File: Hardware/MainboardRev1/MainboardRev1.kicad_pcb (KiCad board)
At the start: 4 copper layers, 92 x 92 mm, 210 parts, among them J1 BACKUP_BATT: 1586038-2, J10 Switch_3, J11 Switch_2, J12 Switch_4, J13 EXTRA_5V, J14 EXTRA_3V3, J2 MAIN_BATT: 1586038-2, J3 Servo_Control, J4 EMATCH_1: 1586038-2, J5 EMATCH_2: 1586038-2, J6 Stratologger_PWR: 1586038-2, J7 Stratologger_DATA, J8 0733910320 [915MHz SMA], J9 Switch_1, Q1 SSM3J328R, Q10 SSM3J328R, Q11 NTR4003, Q12 NTR4003, Q13 NTR4003, Q14 SSM3J328R, Q15 NTR4003, Q16 SSM3J328R, Q17 SSM3J328R, Q18 NTR4003, Q19 NTR4003, Q2 SSM3J328R, Q20 SIS612EDNT-T1-GE3, Q21 SIS612EDNT-T1-GE3, Q22 NTR4003, Q23 NTR4003, Q24 NTR4003, Q25 SSM3J328R, Q26 NTR4003, Q3 SSM3J328R, Q4 SSM3J328R, Q5 NTR4003, Q6 NTR4003, Q7 NTR4003, Q8 SSM3J328R, Q9 NTR4003, SW1 EG2201A [DPDT], U1 LT6703-3, U10 LTC4358, U11 Teensy3.6, U12 ABPMANN030PG2A3, U13 LSM9DS1, U14 LIS331HH, U15 BME280, U16 CCS811, U17 ublox_max-m8q, U18 RFM69HCW, U2 LTC3605, U3 LTC4358, U4 LTC4358, U5 LDL1117S50R, U6 LDL1117S33R, U7 LTC2992, U8 LDL1117S33R, U9 LTC2992

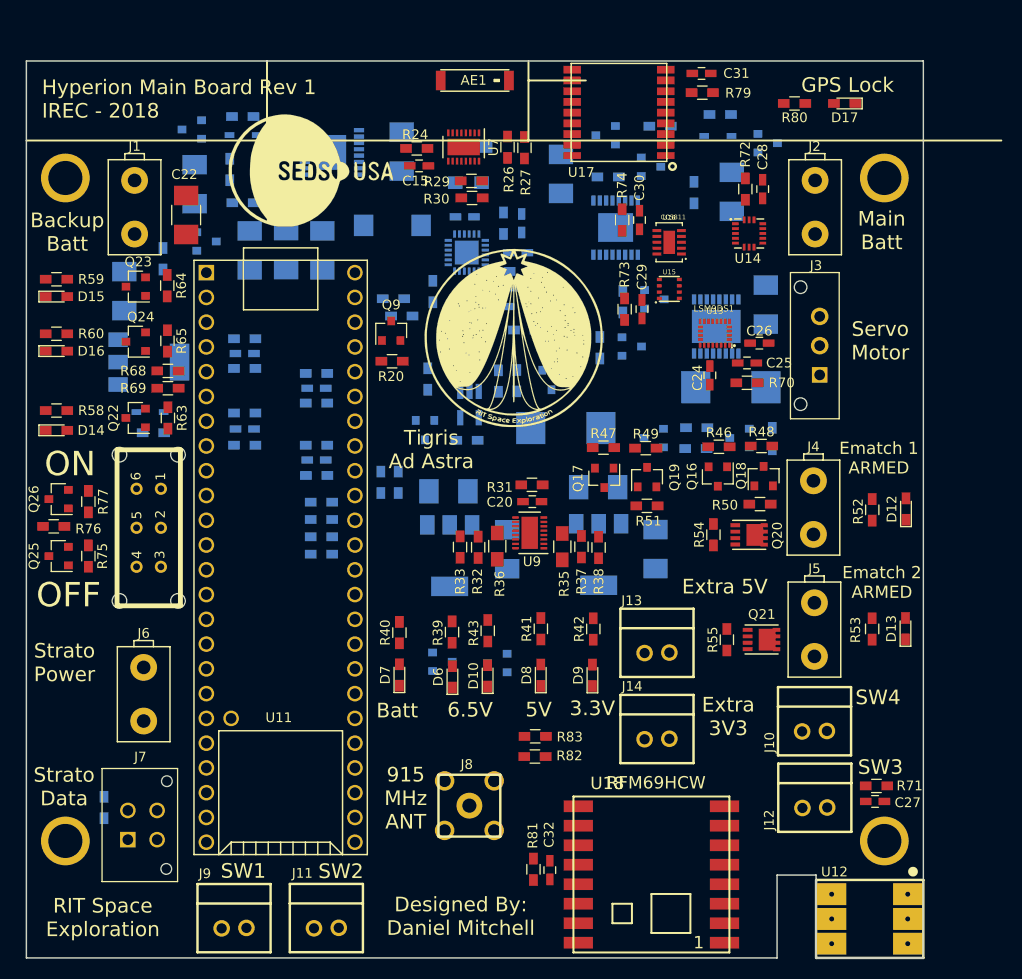
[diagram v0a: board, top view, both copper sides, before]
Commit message: Added buzzer and strobe LED. Created BOM. Reannotated. Added sponsors to silkscreen. Needs to be routed and sent out. Good luck Matt!
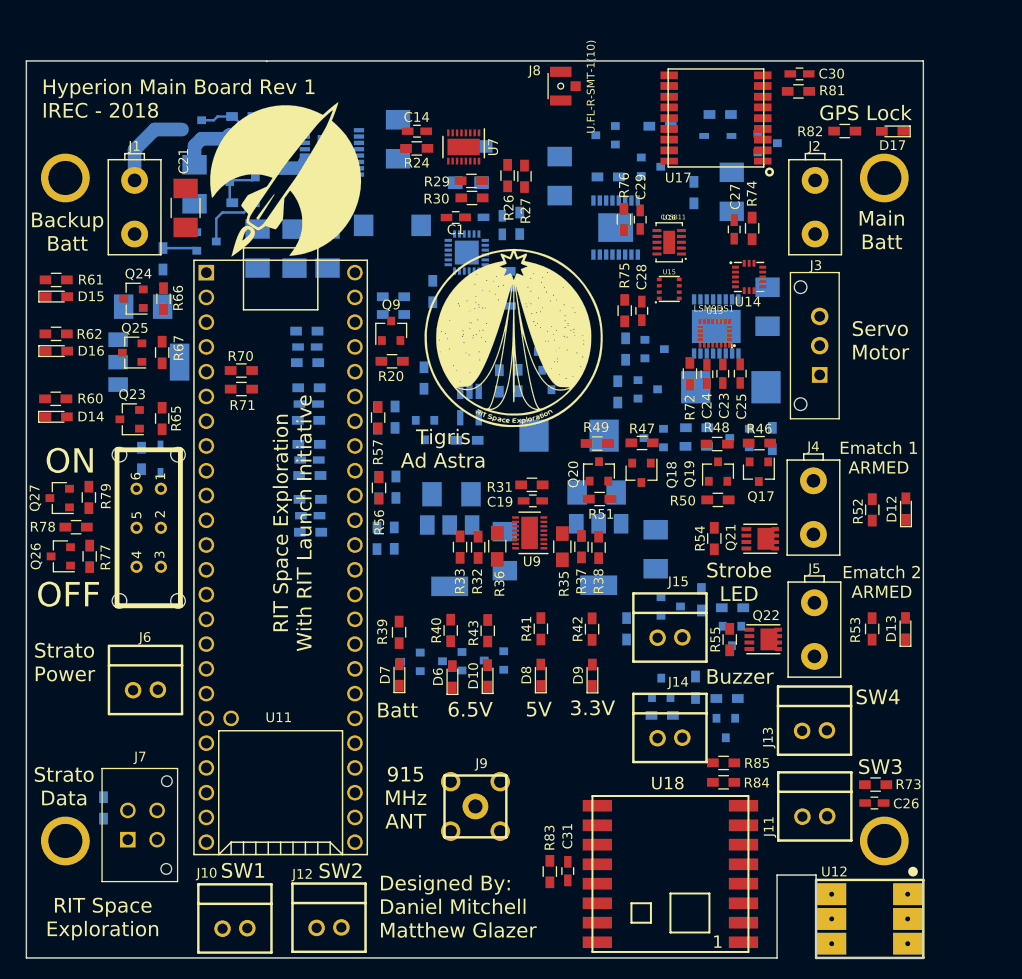
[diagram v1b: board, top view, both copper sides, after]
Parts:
- removed AE1: 1575AT43A0040E, Dans_Parts:ANT_CHIP_OMNI_1575MHz_GPS
- removed C36: 10nF, Capacitors_SMD:C_0603_HandSoldering
- added C1: 0.1uF, Capacitors_SMD:C_0603_HandSoldering, F.Cu at (94.0, 66.1)
- added G***: LOGO, Media:LI_Logo, F.Cu at (76.6, 62.1)
- added J15: Strobe, Dans_Parts:CONN_2POS_VERT_TE_CONN_LOCK_5-103669-1, F.Cu at (116.0, 109.1)
- added Q27: NTR4003, TO_SOT_Packages_SMD:SOT-23, F.Cu at (53.4, 94.8)
- added Q28: SSM3J328R, TO_SOT_Packages_SMD:SOT-23, B.Cu at (121.7, 118.4)
- added Q29: SSM3J328R, TO_SOT_Packages_SMD:SOT-23, B.Cu at (122.4, 109.0)
- added Q30: NTR4003, TO_SOT_Packages_SMD:SOT-23, B.Cu at (115.1, 114.3)
- added Q31: NTR4003, TO_SOT_Packages_SMD:SOT-23, B.Cu at (116.1, 106.0)
- added R92: 1k, Resistors_SMD:R_0603_HandSoldering, B.Cu at (79.0, 89.3)
- added R93: 1k, Resistors_SMD:R_0603_HandSoldering, B.Cu at (78.8, 77.7)
- added R94: 10K, Resistors_SMD:R_0603_HandSoldering, B.Cu at (121.9, 115.4)
- added R95: 10K, Resistors_SMD:R_0603_HandSoldering, B.Cu at (122.4, 106.1)
- added R96: 12k, Resistors_SMD:R_0603_HandSoldering, B.Cu at (118.6, 114.2)
- added R97: 12k, Resistors_SMD:R_0603_HandSoldering, B.Cu at (119.2, 105.3)
- added R98: 10k, Resistors_SMD:R_0603_HandSoldering, B.Cu at (115.2, 117.1)
- added R99: 10k, Resistors_SMD:R_0603_HandSoldering, B.Cu at (111.6, 108.2)
- C14, C19: value 47uF -> 0.1uF; footprint Capacitors_SMD:C_1210_HandSoldering -> Capacitors_SMD:C_0603_HandSoldering; moved to F.Cu
- C15, C20: value 0.1uF -> 47uF; footprint Capacitors_SMD:C_0603_HandSoldering -> Capacitors_SMD:C_1210_HandSoldering; moved to B.Cu
- C21, R84, R85: moved to F.Cu
- C22, G***: moved to B.Cu
- C23: value 47uF -> 10000pF; footprint Capacitors_SMD:C_1210_HandSoldering -> Capacitors_SMD:C_0603_HandSoldering; moved to F.Cu
- C24: value 10000pF -> 0.1uF
- C25: value 0.1uF -> 100nF
- C26: value 100nF -> 0.1uF
- C32: value 0.1uF -> 10nF; moved to B.Cu
- C4: value 0.1uF -> .01uF
- C5: value .01uF -> 0.1uF
- C7: value 0.1uF -> 10pF
- C8: value 10pF -> 220pF
- C9: value 220pF -> 47uF; footprint Capacitors_SMD:C_0603_HandSoldering -> Capacitors_SMD:C_1210_HandSoldering
- D14: value LED -> Green
- D15: value LED -> Blue
- D16: value LED -> Red
- J10: value Switch_3 -> Switch_1
- J11: value Switch_2 -> Switch_3
- J12: value Switch_4 -> Switch_2
- J13: value EXTRA_5V -> Switch_4
- J14: value EXTRA_3V3 -> Buzzer
- J6: footprint Dans_Parts:CONN_2POS_VERT_TE_CONN -> Dans_Parts:CONN_2POS_VERT_TE_CONN_LOCK_5-103669-1
- J8: value 0733910320 [915MHz SMA] -> U.FL-R-SMT-1(10); footprint Dans_Parts:CONN_RP-SMA_Right_Angle_0733910320 -> Dans_Parts:HRS_U.FL-R-SMT-1(10)
- J9: value Switch_1 -> 0733910320 [915MHz SMA]; footprint Dans_Parts:CONN_2POS_VERT_TE_CONN_LOCK_5-103669-1 -> Dans_Parts:CONN_RP-SMA_Right_Angle_0733910320
- Q14, Q25: value SSM3J328R -> NTR4003
- Q15, Q18, Q26: value NTR4003 -> SSM3J328R
- Q16: value SSM3J328R -> NTR4003; moved to B.Cu
- Q20: value SIS612EDNT-T1-GE3 -> NTR4003; footprint Dans_Parts:PowerPAK_1212-8S -> TO_SOT_Packages_SMD:SOT-23
- Q22: value NTR4003 -> SIS612EDNT-T1-GE3; footprint TO_SOT_Packages_SMD:SOT-23 -> Dans_Parts:PowerPAK_1212-8S
- R14, R9: value 500 -> 510
- R39, R40, R42, R60: value R -> 80
- R41: value R -> 470
- R43: value R -> 150
- R52, R53: value R -> 510
- R56: value 45.2k -> 1M; moved to F.Cu
- R57: value 11.3k -> 1M; moved to F.Cu
- R58: value R -> 45.3k; moved to B.Cu
- R59: value R -> 11.3k; moved to B.Cu
- R61: value 45.2k -> 80; moved to F.Cu
- R62: value 11.3k -> 150; moved to F.Cu
- R63, R68: value 10k -> 45.3k; moved to B.Cu
- R64, R69: value 10k -> 11.3k; moved to B.Cu
- R66: value 45.2k -> 10k; moved to F.Cu
- R67: value 11.3k -> 10k; moved to F.Cu
- R70, R71, R79: value 10 -> 10k
- R75, R83: value 10k -> 10
- R76: value 12k -> 10
- R78: value 0 -> 12k; moved to F.Cu
- R80: value R -> 0; moved to B.Cu
- R82: value 10k -> 80
- R86, R87, R90, R91: value 1k -> 10k
- R88, R89: value 10k -> 1k
- moved R80 101.2 mm to (57.9, 126.6), turned to 90 degrees
- moved R81 84.3 mm to (129.2, 53.1), turned to 0 degrees
- moved C31 83.0 mm to (105.5, 133.1), turned to 90 degrees
- moved R71 76.8 mm to (72.1, 83.7), turned to 180 degrees
- moved R79 75.4 mm to (56.4, 94.8), turned to 90 degrees
- moved J8 74.4 mm to (104.8, 52.6), turned to 90 degrees
- moved R82 71.6 mm to (133.9, 57.2)
- moved Q22 66.6 mm to (124.2, 108.3), turned to 0 degrees
- moved R76 66.4 mm to (111.3, 66.3), turned to 90 degrees
- moved J10 62.8 mm to (71.4, 138.9)
- moved G*** 61.0 mm to (101.7, 117.9), turned to 180 degrees
- moved R75 60.5 mm to (111.4, 75.6)
- moved C27 60.4 mm to (122.6, 67.3), turned to 90 degrees
- moved C22 60.4 mm to (126.0, 75.2)
- moved R85 55.7 mm to (121.5, 122.0), turned to 0 degrees
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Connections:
- C11 pad 1: +6.5V_MSMT -> BATTERY_PWR_MSMT
- C12 pad 1: BATTERY_PWR_MSMT -> +6.5V_MSMT
- C13 pad 1: +6.5V_MSMT -> BATTERY_PWR_MSMT
- C14 pad 1: BATTERY_PWR_MSMT -> Net-(C14-Pad1)
- C15 pad 1: Net-(C15-Pad1) -> LDO_FEED
- C17 pad 1: LDO_FEED -> +5V_MSMT
- C18 pad 1: +5V_MSMT -> +3.3V_MSMT
- C19 pad 1: +3.3V_MSMT -> Net-(C19-Pad1)
- C20 pad 1: Net-(C20-Pad1) -> STARTUP_BATT
- C21 pad 1: STARTUP_BATT -> +3.3V_STARTUP
- C22 pad 1: +3.3V_STARTUP -> Net-(C22-Pad1)
- C23 pad 1: Net-(C23-Pad1) -> LSM_CAP
- C24 pad 1: LSM_CAP -> Net-(C24-Pad1)
- C25 pad 1: Net-(C25-Pad1) -> LSM_C1
- C26 pad 1: LSM_C1 -> Net-(C26-Pad1)
- C4 pad 1: BATTERY_PWR -> Net-(C4-Pad1)
- C5 pad 1: Net-(C5-Pad1) -> GND
- C5 pad 2: GND -> SVIN
- C6 pad 1: GND -> Net-(C6-Pad1)
- C6 pad 2: SVIN -> Net-(C6-Pad2)
- C7 pad 2: Net-(C7-Pad2) -> GND
- C9 pad 1: Net-(C9-Pad1) -> +6.5V_MSMT
- D11 pad 1: Net-(C23-Pad1) -> Net-(C22-Pad1)
- D3 pad 1: Net-(C7-Pad1) -> Net-(C6-Pad1)
- D7 pad 1: GND -> Net-(D7-Pad1)
- J10 pad 1: Net-(C34-Pad1) -> Net-(C32-Pad1)
- J11 pad 1: Net-(C35-Pad1) -> Net-(C33-Pad1)
- J12 pad 1: Net-(C36-Pad1) -> Net-(C34-Pad1)
- J13 pad 1: GND -> Net-(C35-Pad1)
- J13 pad 2: +5V -> GND
- J14 pad 1: GND -> Net-(J14-Pad1)
- J14 pad 2: +3.3V -> GND
- J3 pad 2: Net-(C23-Pad1) -> Net-(C22-Pad1)
- J9 pad 1: Net-(C33-Pad1) -> Net-(J9-Pad1)
- L1 pad 1: Net-(C7-Pad2) -> Net-(C6-Pad2)
- Q13 pad 1: CONTROL_2 -> +3.3V
- Q13 pad 3: Net-(D10-Pad1) -> Net-(D7-Pad1)
- Q14 pad 1: Net-(Q14-Pad1) -> CONTROL_2
- Q14 pad 2: +6.5V -> GND
- Q14 pad 3: Net-(Q14-Pad3) -> Net-(D10-Pad1)
- Q15 pad 1: SERVO_PWR_EN -> Net-(Q15-Pad1)
- Q15 pad 2: GND -> +6.5V
- Q15 pad 3: Net-(Q14-Pad1) -> Net-(Q15-Pad3)
- Q16 pad 1: Net-(Q16-Pad1) -> SERVO_PWR_EN
- Q16 pad 2: BATTERY_PWR -> GND
- Q16 pad 3: Net-(J4-Pad1) -> Net-(Q15-Pad1)
- Q17 pad 3: Net-(J5-Pad1) -> Net-(J4-Pad1)
- Q18 pad 1: EMATCH_1_ARM -> Net-(Q18-Pad1)
- Q18 pad 2: GND -> BATTERY_PWR
- Q18 pad 3: Net-(Q18-Pad3) -> Net-(J5-Pad1)
- Q19 pad 1: EMATCH_2_ARM -> EMATCH_1_ARM
- Q20 pad 1: EMATCH_1_FIRE -> EMATCH_2_ARM
- Q20 pad 3: EMATCH_1_CHECK -> Net-(Q20-Pad3)
- Q21 pad 1: EMATCH_2_FIRE -> EMATCH_1_FIRE
- Q21 pad 3: EMATCH_2_CHECK -> EMATCH_1_CHECK
- Q22 pad 1: LED_GREEN -> EMATCH_2_FIRE
- Q22 pad 3: Net-(D14-Pad1) -> EMATCH_2_CHECK
- Q23 pad 1: LED_BLUE -> LED_GREEN
- Q23 pad 3: Net-(D15-Pad1) -> Net-(D14-Pad1)
- Q24 pad 1: LED_RED -> LED_BLUE
- Q24 pad 3: Net-(D16-Pad1) -> Net-(D15-Pad1)
- Q25 pad 1: Net-(Q25-Pad1) -> LED_RED
- Q25 pad 2: BACKUP_BATT -> GND
- Q25 pad 3: Net-(J6-Pad1) -> Net-(D16-Pad1)
- Q26 pad 1: +3.3V_STARTUP -> Net-(Q26-Pad1)
- Q26 pad 2: GND -> BACKUP_BATT
- Q26 pad 3: Net-(Q26-Pad3) -> Net-(J6-Pad1)
- R15 pad 1: Net-(C9-Pad1) -> Net-(C8-Pad1)
- R15 pad 2: Net-(C8-Pad1) -> Net-(C7-Pad1)
- R24 pad 1: Net-(C15-Pad1) -> Net-(C14-Pad1)
- R31 pad 1: Net-(C20-Pad1) -> Net-(C19-Pad1)
- R39 pad 1: +5V -> Net-(D7-Pad2)
- R39 pad 2: Net-(D6-Pad2) -> +5V
- R40 pad 1: Net-(D7-Pad2) -> +5V
- R40 pad 2: BATTERY_PWR -> Net-(D6-Pad2)
- R41 pad 2: +5V -> BATTERY_PWR
- R42 pad 2: +3.3V -> +5V
- R44 pad 2: Net-(Q14-Pad1) -> Net-(Q15-Pad1)
- R46 pad 2: Net-(Q16-Pad1) -> Net-(Q17-Pad1)
- R47 pad 2: Net-(Q17-Pad1) -> Net-(Q18-Pad1)
- R48 pad 1: Net-(Q16-Pad1) -> Net-(Q17-Pad1)
- R48 pad 2: Net-(Q18-Pad3) -> Net-(Q19-Pad3)
- R49 pad 1: Net-(Q17-Pad1) -> Net-(Q18-Pad1)
- R49 pad 2: Net-(Q19-Pad3) -> Net-(Q20-Pad3)
- R56 pad 1: MAIN_BATT -> EMATCH_1_CHECK
- R56 pad 2: MAIN_BATT_ANLG -> GND
- R57 pad 1: MAIN_BATT_ANLG -> EMATCH_2_CHECK
- R57 pad 2: MAIN_BATT_READ_EN -> GND
- R58 pad 1: Net-(D14-Pad2) -> MAIN_BATT
- R58 pad 2: +5V -> MAIN_BATT_ANLG
- R59 pad 1: Net-(D15-Pad2) -> MAIN_BATT_ANLG
- R59 pad 2: +5V -> MAIN_BATT_READ_EN
- R60 pad 1: Net-(D16-Pad2) -> Net-(D14-Pad2)
- R61 pad 1: EMATCH_1_CHECK -> Net-(D15-Pad2)
- R61 pad 2: EMATCH_1_ANLG -> +5V
- R62 pad 1: EMATCH_1_ANLG -> Net-(D16-Pad2)
- R62 pad 2: GND -> +5V
- R63 pad 1: GND -> EMATCH_1_CHECK
- R63 pad 2: LED_GREEN -> EMATCH_1_ANLG
- R64 pad 1: GND -> EMATCH_1_ANLG
- R64 pad 2: LED_BLUE -> GND
- R65 pad 1: +3.3V -> GND
- R65 pad 2: LED_RED -> LED_GREEN
- R66 pad 1: EMATCH_2_CHECK -> GND
- R66 pad 2: EMATCH_2_ANLG -> LED_BLUE
- R67 pad 1: EMATCH_2_ANLG -> +3.3V
- R67 pad 2: GND -> LED_RED
- R68 pad 1: +3.3V -> EMATCH_2_CHECK
- R68 pad 2: SENSORS_SCL -> EMATCH_2_ANLG
- R69 pad 1: +3.3V -> EMATCH_2_ANLG
- R69 pad 2: SENSORS_SDA -> GND
- R70 pad 1: Net-(C25-Pad1) -> +3.3V
- R70 pad 2: +3.3V -> SENSORS_SCL
- R71 pad 1: Net-(C27-Pad1) -> +3.3V
- R71 pad 2: +3.3V -> SENSORS_SDA
- R72 pad 1: Net-(C28-Pad1) -> Net-(C24-Pad1)
- R73 pad 1: Net-(C29-Pad1) -> Net-(C26-Pad1)
- R74 pad 1: Net-(C30-Pad1) -> Net-(C27-Pad1)
- R75 pad 1: BACKUP_BATT -> Net-(C28-Pad1)
- R75 pad 2: Net-(Q25-Pad1) -> +3.3V
- R76 pad 1: Net-(Q25-Pad1) -> Net-(C29-Pad1)
- R76 pad 2: Net-(Q26-Pad3) -> +3.3V
- R77 pad 1: +3.3V_STARTUP -> BACKUP_BATT
- R77 pad 2: GND -> Net-(Q26-Pad1)
- R78 pad 1: Net-(J7-Pad1) -> Net-(Q26-Pad1)
- R78 pad 2: +3.3V -> Net-(Q27-Pad3)
- R79 pad 1: Net-(C31-Pad1) -> +3.3V_STARTUP
- R79 pad 2: +3.3V -> GND
- R80 pad 1: Net-(D17-Pad2) -> Net-(J7-Pad1)
- R80 pad 2: Net-(R80-Pad2) -> +3.3V
- R81 pad 1: Net-(C32-Pad1) -> Net-(C30-Pad1)
- R82 pad 1: +3.3V -> Net-(D17-Pad2)
- R82 pad 2: COMMS_CS_LORA -> Net-(R82-Pad2)
- R83 pad 1: +3.3V -> Net-(C31-Pad1)
- R83 pad 2: LORA_RESET -> +3.3V
- R84 pad 2: Net-(C33-Pad1) -> COMMS_CS_LORA
- R85 pad 2: Net-(C34-Pad1) -> LORA_RESET
- R86 pad 1: SWITCH_1 -> +3.3V
- R86 pad 2: Net-(C33-Pad1) -> Net-(C32-Pad1)
- R87 pad 1: SWITCH_3 -> +3.3V
- R87 pad 2: Net-(C34-Pad1) -> Net-(C33-Pad1)
- R88 pad 1: +3.3V -> SWITCH_1
- R88 pad 2: Net-(C35-Pad1) -> Net-(C32-Pad1)
- R89 pad 1: +3.3V -> SWITCH_3
- R89 pad 2: Net-(C36-Pad1) -> Net-(C33-Pad1)
- R90 pad 1: SWITCH_2 -> +3.3V
- R90 pad 2: Net-(C35-Pad1) -> Net-(C34-Pad1)
- R91 pad 1: SWITCH_4 -> +3.3V
- R91 pad 2: Net-(C36-Pad1) -> Net-(C35-Pad1)
- U10 pad 1: Net-(Q14-Pad3) -> Net-(Q15-Pad3)
- U10 pad 10: Net-(C23-Pad1) -> Net-(C22-Pad1)
- U10 pad 12: Net-(Q14-Pad3) -> Net-(Q15-Pad3)
- U10 pad 13: Net-(Q14-Pad3) -> Net-(Q15-Pad3)
- U10 pad 14: Net-(Q14-Pad3) -> Net-(Q15-Pad3)
- U10 pad 15: Net-(Q14-Pad3) -> Net-(Q15-Pad3)
- U10 pad 16: Net-(Q14-Pad3) -> Net-(Q15-Pad3)
- U10 pad 17: Net-(C23-Pad1) -> Net-(C22-Pad1)
- U10 pad 2: Net-(Q14-Pad3) -> Net-(Q15-Pad3)
- U10 pad 3: Net-(Q14-Pad3) -> Net-(Q15-Pad3)
- U10 pad 4: Net-(Q14-Pad3) -> Net-(Q15-Pad3)
- U10 pad 9: Net-(C23-Pad1) -> Net-(C22-Pad1)
- U11 pad 34: DATA_READY -> Buzzer_Disable
- U11 pad 35: DATA_READY_1 -> Strobe_Disable
- U12 pad 2: Net-(C27-Pad1) -> Net-(C26-Pad1)
- U13 pad 1: Net-(C25-Pad1) -> Net-(C24-Pad1)
- U13 pad 22: Net-(C25-Pad1) -> Net-(C24-Pad1)
- U13 pad 23: Net-(C25-Pad1) -> Net-(C24-Pad1)
- U13 pad 3: Net-(C25-Pad1) -> Net-(C24-Pad1)
- U14 pad 1: Net-(C28-Pad1) -> Net-(C27-Pad1)
- U14 pad 14: Net-(C28-Pad1) -> Net-(C27-Pad1)
- U14 pad 15: Net-(C28-Pad1) -> Net-(C27-Pad1)
- U15 pad 2: Net-(C29-Pad1) -> Net-(C28-Pad1)
- U15 pad 6: Net-(C29-Pad1) -> Net-(C28-Pad1)
- U15 pad 8: Net-(C29-Pad1) -> Net-(C28-Pad1)
- U16 pad 6: Net-(C30-Pad1) -> Net-(C29-Pad1)
- U17 pad 11: Net-(AE1-Pad1) -> Net-(J8-Pad1)
- U17 pad 4: Net-(R80-Pad2) -> Net-(R82-Pad2)
- U17 pad 6: Net-(C31-Pad1) -> Net-(C30-Pad1)
- U17 pad 7: Net-(C31-Pad1) -> Net-(C30-Pad1)
- U17 pad 8: Net-(C31-Pad1) -> Net-(C30-Pad1)
- U17 pad 9: Net-(C31-Pad1) -> Net-(C30-Pad1)
- U18 pad 13: Net-(C32-Pad1) -> Net-(C31-Pad1)
- U18 pad 9: Net-(J8-Pad1) -> Net-(J9-Pad1)
- U2 pad 11: Net-(C7-Pad2) -> Net-(C6-Pad2)
- U2 pad 12: Net-(C7-Pad2) -> Net-(C6-Pad2)
- U2 pad 13: Net-(C7-Pad2) -> Net-(C6-Pad2)
- U2 pad 14: Net-(C7-Pad2) -> Net-(C6-Pad2)
- U2 pad 15: Net-(C7-Pad2) -> Net-(C6-Pad2)
- U2 pad 16: Net-(C7-Pad2) -> Net-(C6-Pad2)
- U2 pad 20: Net-(C7-Pad1) -> Net-(C6-Pad1)
- U2 pad 5: Net-(C5-Pad1) -> Net-(C4-Pad1)
- U2 pad 6: Net-(C8-Pad1) -> Net-(C7-Pad1)
- U7 pad 4: DATA_READY -> Net-(U7-Pad4)
- U7 pad 7: Net-(C15-Pad1) -> Net-(C14-Pad1)
- U7 pad 8: Net-(C15-Pad1) -> Net-(C14-Pad1)
- U9 pad 4: DATA_READY_1 -> Net-(U9-Pad4)
- U9 pad 7: Net-(C20-Pad1) -> Net-(C19-Pad1)
- U9 pad 8: Net-(C20-Pad1) -> Net-(C19-Pad1)
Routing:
- net BACKUP_BATT: track 0.00 -> 11.1 mm
- net Net-(J1-Pad1): track 0.00 -> 8.88 mm
- net Net-(Q5-Pad3): track 0.00 -> 6.86 mm
- net Net-(D1-Pad2): track 0.00 -> 6.60 mm
- net GND: track 0.00 -> 5.86 mm
- net Net-(Q3-Pad1): track 0.00 -> 5.17 mm
- net Net-(Q3-Pad3): track 0.00 -> 5.03 mm
- net BACKUP_BATT_EN: track 0.00 -> 3.58 mm
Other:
- board text added: "Buzzer"
- board text added: "Designed By: Daniel Mitchell Matthew Glazer"
- board text added: "RIT Space Exploration With RIT Launch Initiative"
- board text added: "Sponsored By: SEDS USA Matthew Glazer Samuel Carlson SPEXcast"
- board text added: "Strobe LED"
- board text removed: "Designed By: Daniel Mitchell"
- board text removed: "Extra 3V3"
- board text removed: "Extra 5V"

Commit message: started routing PCB
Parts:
- moved R10 1.76 mm to (70.9, 65.7), turned to 270 degrees
- moved Q5 0.30 mm to (68.2, 68.4)
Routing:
- net Net-(C26-Pad1): track 0.00 -> 21.9 mm
- net Net-(J6-Pad1): track 0.00 -> 19.6 mm
- net BACKUP_BATT: track 11.1 -> 21.1 mm
- net Net-(D15-Pad1): track 0.00 -> 8.80 mm
- net Net-(D14-Pad1): track 0.00 -> 8.62 mm
- net Net-(D16-Pad1): track 0.00 -> 8.60 mm
- net Net-(R82-Pad2): track 0.00 -> 7.40 mm
- net Net-(Q27-Pad3): track 0.00 -> 5.73 mm
- net Net-(Q26-Pad1): track 0.00 -> 4.62 mm
- net Net-(Q5-Pad3): track 6.86 -> 2.36 mm
- net Net-(J7-Pad1): track 0.00 -> 4.32 mm
- net Net-(D12-Pad2): track 0.00 -> 3.49 mm
- net Net-(D13-Pad2): track 0.00 -> 3.43 mm
- net Net-(D17-Pad2): track 0.00 -> 2.72 mm
- net +3.3V_STARTUP: track 0.00 -> 2.03 mm
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
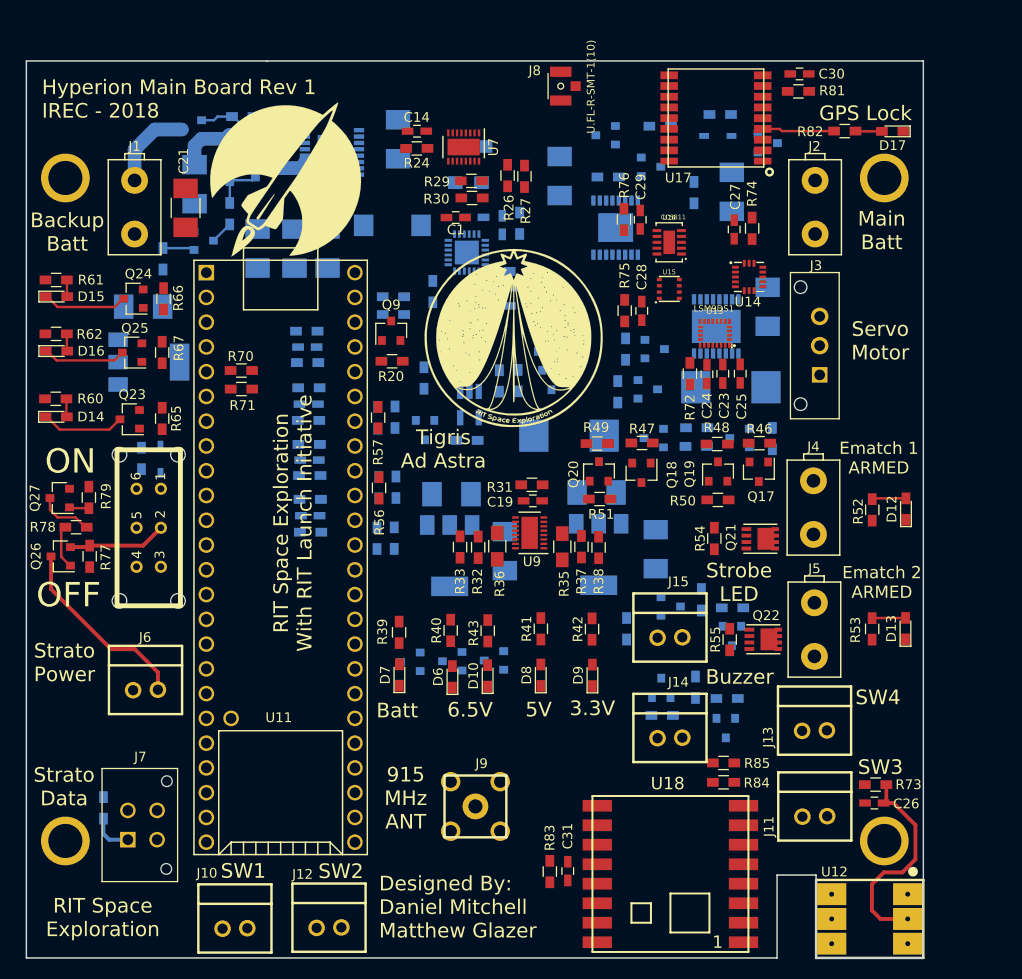
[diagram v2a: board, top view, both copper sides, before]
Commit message: continued work on routing, plenty of work still to be done
commiting my work for the night
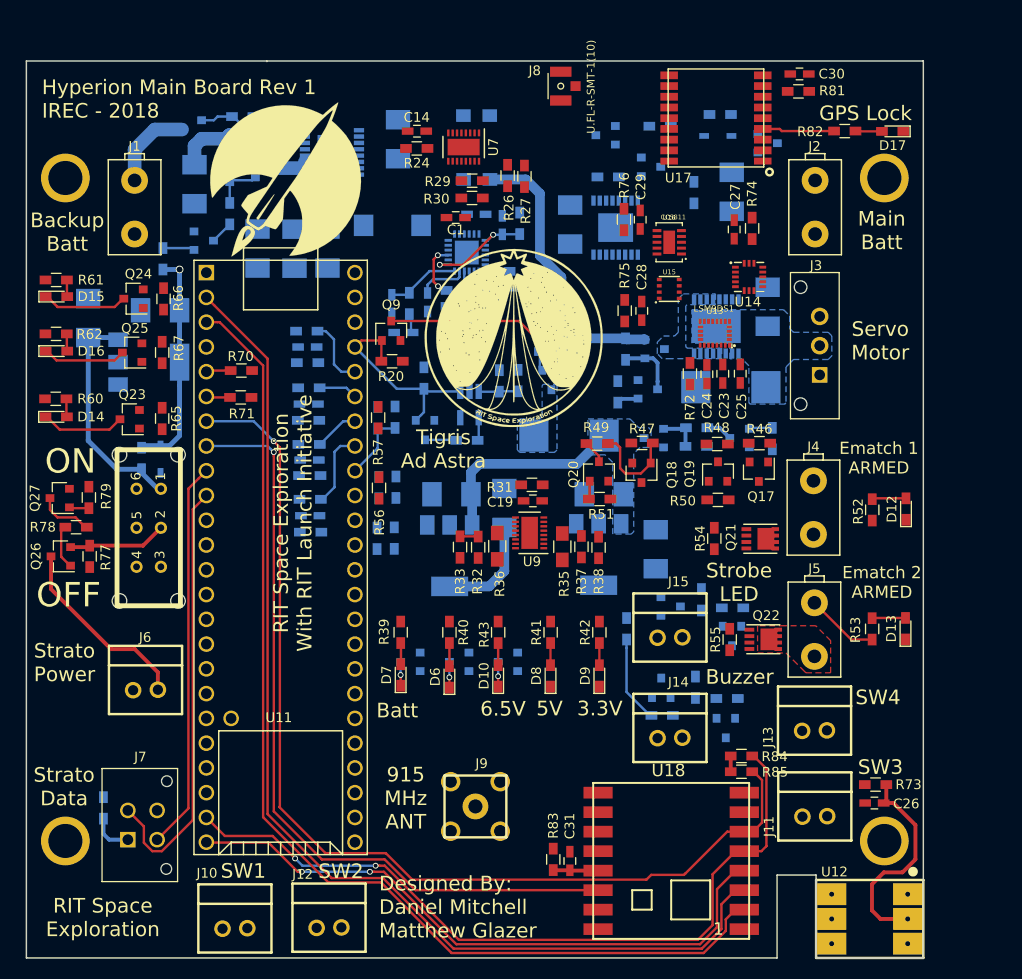
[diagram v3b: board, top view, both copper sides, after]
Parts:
- C21: moved to B.Cu
- moved C21 10.8 mm to (63.7, 75.6), turned to 180 degrees
- moved C4 7.52 mm to (91.2, 74.8), turned to 270 degrees
- moved R19 7.05 mm to (94.2, 76.8), turned to 0 degrees
- moved R18 6.60 mm to (94.2, 75.2)
- moved C7 6.40 mm to (87.5, 74.9)
- moved R15 6.40 mm to (89.3, 74.9)
- moved C20 5.76 mm to (56.3, 76.4), turned to 90 degrees
- moved C8 5.63 mm to (88.7, 77.8)
- moved C13 5.09 mm to (105.8, 66.8)
- moved C17 4.43 mm to (99.0, 95.8)
- moved R84 3.27 mm to (123.3, 121.3)
- moved R25 3.20 mm to (96.2, 55.6)
- moved R17 2.51 mm to (94.2, 73.5), turned to 0 degrees
- moved R85 2.04 mm to (123.3, 122.9)
- moved Q14 1.44 mm to (99.4, 111.6)
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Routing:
- net COMMS_MOSI: track 0.00 -> 114.2 mm
- net COMMS_MISO: track 0.00 -> 111.6 mm
- net LORA_RESET: track 0.00 -> 106.3 mm, vias 0 -> 1
- net LORA_INT: track 0.00 -> 80.6 mm, vias 0 -> 1
- net COMMS_CS_LORA: track 0.00 -> 79.2 mm, vias 0 -> 2
- net COMMS_SCLK: track 0.00 -> 64.9 mm, vias 0 -> 2
- net SENSORS_TX: track 0.00 -> 44.6 mm
- net SENSORS_RX: track 0.00 -> 39.9 mm
- net +3.3V_STARTUP: track 2.03 -> 36.5 mm, vias 0 -> 1
- net +6.5V: track 0.00 -> 33.4 mm
- net STARTUP_BATT: track 0.00 -> 23.5 mm
- net CONTROL_1: track 0.00 -> 21.5 mm
- net LDO_FEED: track 0.00 -> 20.7 mm
- net Net-(Q8-Pad1): track 0.00 -> 19.1 mm, vias 0 -> 1
- net SVIN: track 0.00 -> 11.4 mm, vias 0 -> 2
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- added copper zone on F.Cu, net EMATCH_2_CHECK
- added copper zone on B.Cu, net LDO_FEED
- added copper zone on B.Cu, net Net-(C22-Pad1)
- added copper zone on B.Cu, net Net-(D4-Pad2)
- added copper zone on B.Cu, net Net-(Q15-Pad3)

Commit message: morning work, continued routing
shifted some components slightly for better trace routing, so far so good
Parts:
- moved R33 12.8 mm to (107.3, 99.3), turned to 0 degrees
- moved R38 12.6 mm to (96.1, 99.3), turned to 180 degrees
- moved C18 11.2 mm to (103.5, 101.8)
- moved R32 11.2 mm to (107.3, 97.6), turned to 180 degrees
- moved R37 11.1 mm to (96.1, 97.6), turned to 0 degrees
- moved C17 6.06 mm to (98.8, 101.9)
- moved R46 3.77 mm to (122.3, 91.6), turned to 90 degrees
- moved R47 3.36 mm to (111.4, 92.1), turned to 90 degrees
- moved R35 2.69 mm to (104.4, 102.5), turned to 0 degrees
- moved R36 2.59 mm to (97.9, 102.3), turned to 180 degrees
- moved R50 1.59 mm to (119.4, 95.4)
- moved Q19 1.59 mm to (119.4, 92.5)
- moved R48 1.59 mm to (119.3, 89.7)
- moved Q18 1.11 mm to (114.2, 92.0), turned to 0 degrees
- moved Q17 0.61 mm to (125.1, 91.5), turned to 0 degrees
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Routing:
- net EMATCH_1_ARM: track 0.00 -> 61.6 mm, vias 0 -> 1
- net EMATCH_1_FIRE: track 0.00 -> 55.8 mm
- net Net-(J4-Pad1): track 0.00 -> 13.0 mm
- net +3.3V_MSMT: track 0.00 -> 11.5 mm, vias 0 -> 1
- net +5V: track 0.00 -> 7.85 mm, vias 0 -> 1
- net +3.3V: track 1.61 -> 9.01 mm, vias 0 -> 1
- net Net-(Q18-Pad1): track 9.52 -> 4.37 mm
- net +3.3V_DIVIDER: track 0.00 -> 4.78 mm
- net MAIN_BATT_ANLG: track 0.00 -> 4.35 mm
- net EMATCH_1_ANLG: track 0.00 -> 4.34 mm
- net Net-(Q17-Pad1): track 0.00 -> 4.10 mm
- net Net-(C32-Pad1): track 0.00 -> 3.48 mm
- net Net-(C33-Pad1): track 0.00 -> 3.46 mm
- net Net-(C35-Pad1): track 0.00 -> 3.37 mm
- net Net-(C34-Pad1): track 0.00 -> 3.32 mm
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- added copper zone on F.Cu, net Net-(C19-Pad1)
